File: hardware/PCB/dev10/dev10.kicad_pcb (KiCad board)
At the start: 2 copper layers, 13 parts, among them P1 Power, P2 Audio, SW1 WifiRst, U1 LM1117-3.3, U2 ESP-07v2

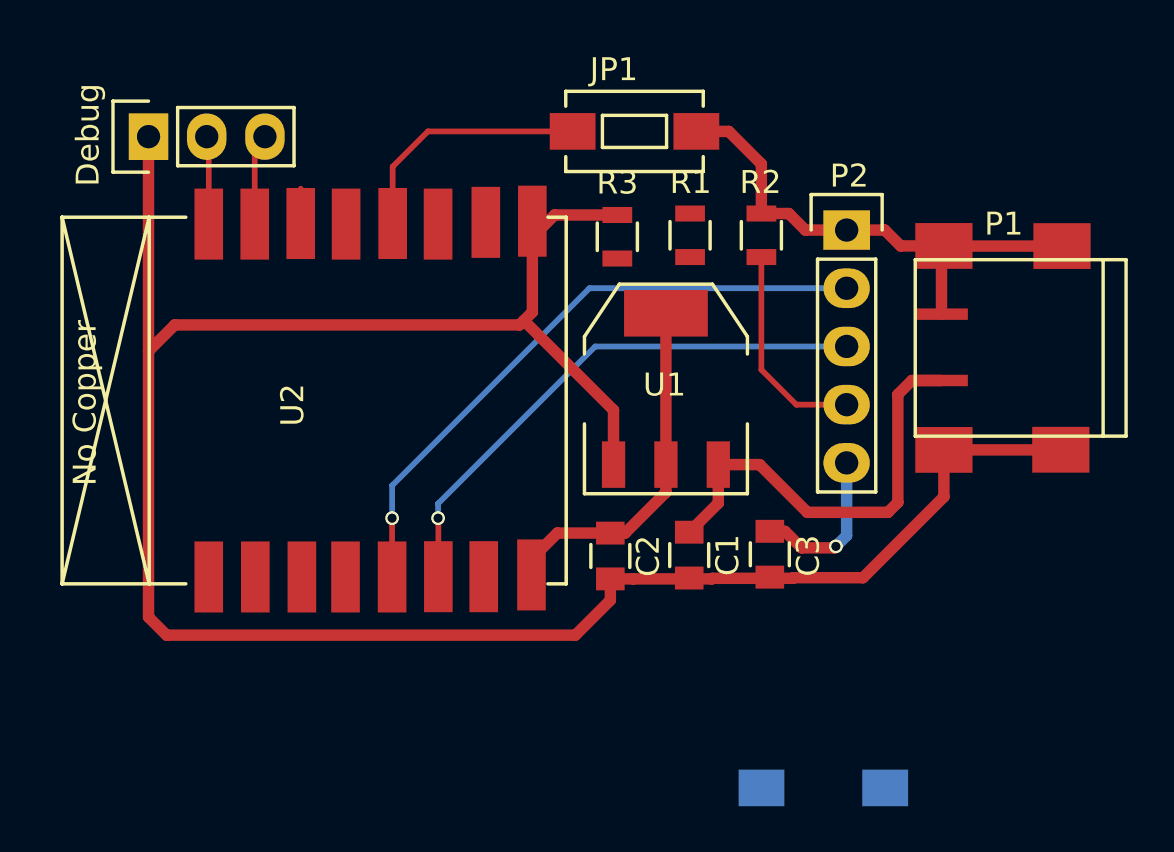
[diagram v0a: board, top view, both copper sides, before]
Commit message: Uppdatering av audiomodul
Grymt mycket bättre ljud!
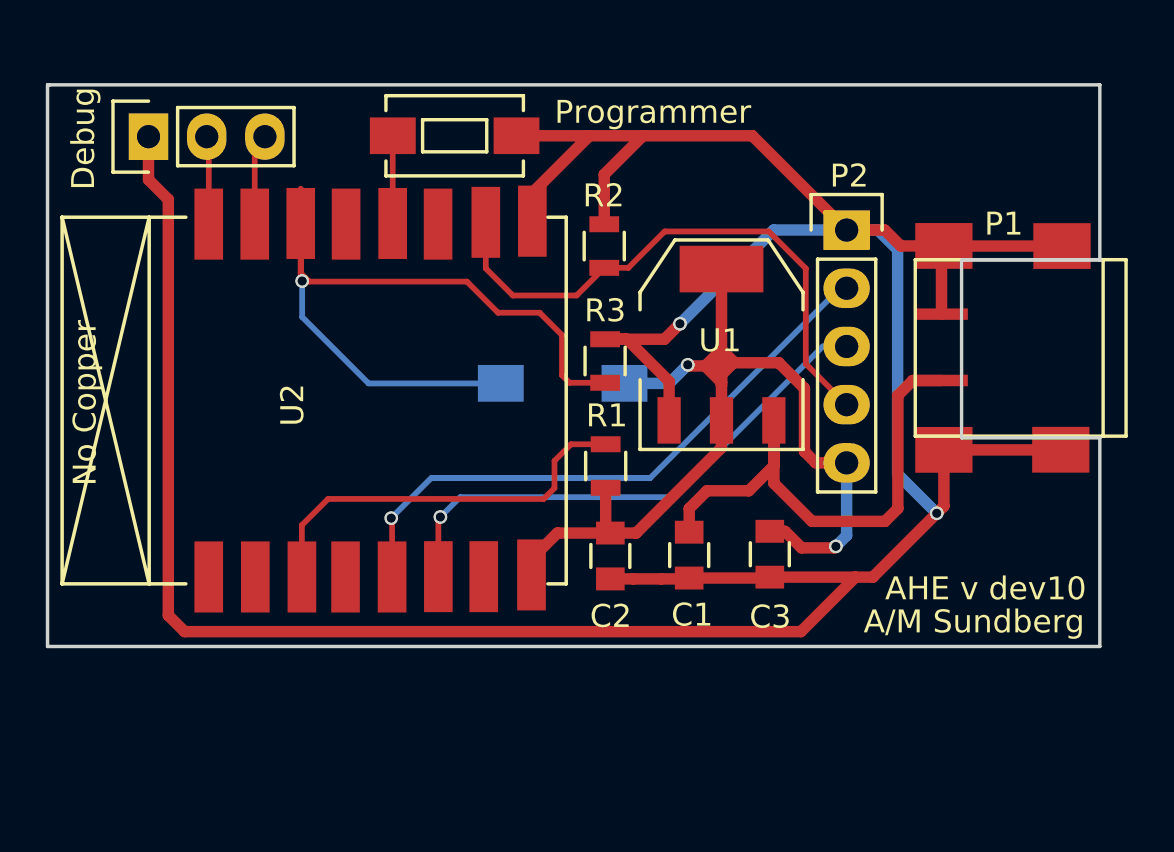
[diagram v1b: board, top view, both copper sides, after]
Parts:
- moved SW1 21.0 mm to (181.7, 104.0)
- moved R1 10.7 mm to (183.6, 107.6), turned to 270 degrees
- moved Programmer 7.85 mm to (177.0, 93.2)
- moved R2 6.87 mm to (183.5, 98.0)
- moved R3 5.45 mm to (183.5, 103.0)
- moved U1 3.10 mm to (188.6, 102.3)
- renumbered JP1 to Programmer
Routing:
- net Net-(R3-Pad2): track 2.22 -> 33.3 mm, vias 0 -> 1
- net GND: track 121.3 -> 147.4 mm, vias 0 -> 2
- net VCC: track 21.9 -> 45.0 mm, vias 1 -> 2
- net Net-(R1-Pad1): track 0.00 -> 17.0 mm
- net SS: track 9.27 -> 24.3 mm
- net Net-(JP1-Pad1): track 11.7 -> 4.53 mm
- net +5V: track 19.2 -> 23.7 mm
- net SCLK: track 26.7 -> 25.9 mm
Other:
- board outline added: 45.9 x 24.5 mm
- board text added: "A/M Sundberg"
- board text added: "AHE v dev10"
